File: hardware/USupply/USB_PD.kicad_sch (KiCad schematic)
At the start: 10 parts, among them Q1 Si2319CDS, U1 HUSB238

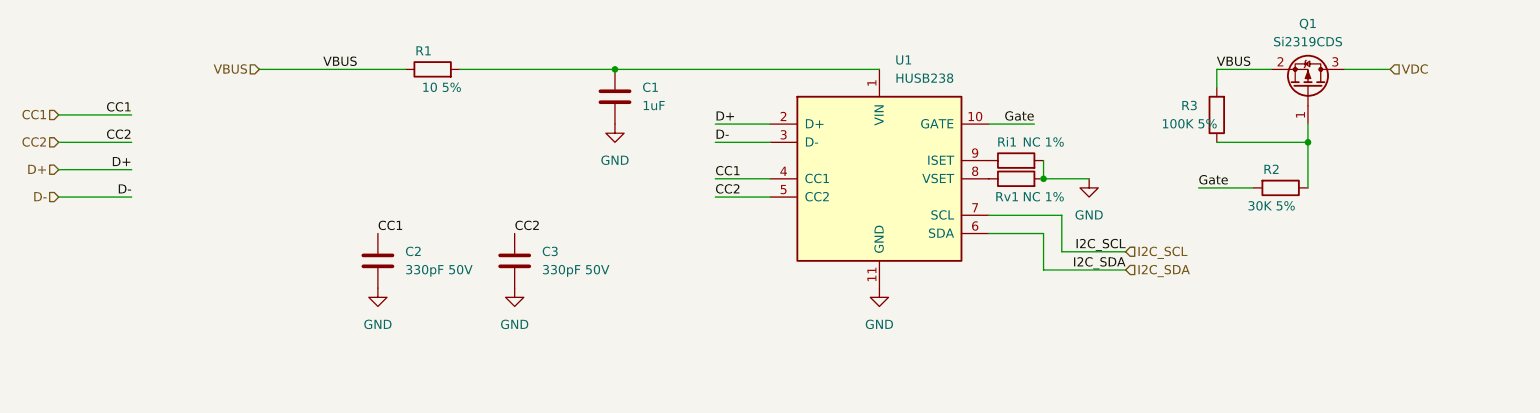
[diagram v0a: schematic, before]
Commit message: feat(hw/usb): update usb pd circuit
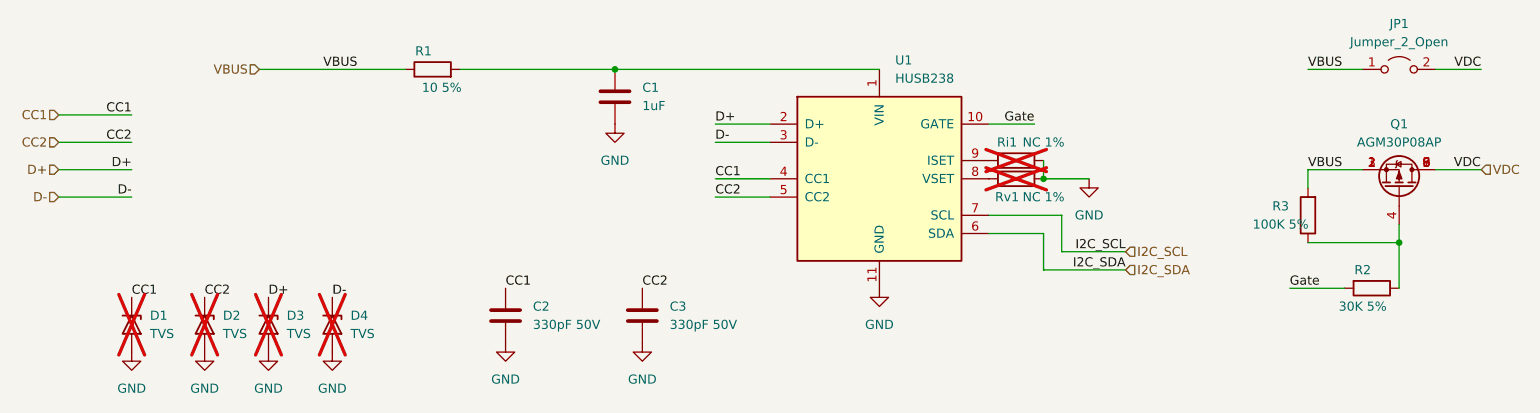
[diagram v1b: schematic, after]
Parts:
- added D1, D2, D3, D4: TVS, Diode_SMD:D_SOD-323, symbol Diode:SM6T22A
- added JP1: Jumper_2_Open, Jumper:SolderJumper-2_P1.3mm_Open_RoundedPad1.0x1.5mm, symbol Jumper:Jumper_2_Open
- Q1: value Si2319CDS -> AGM30P08AP; footprint Package_TO_SOT_SMD:SOT-23 -> Package_DFN_QFN:DFN-8-1EP_3x3mm_P0.65mm_EP1.55x2.4mm
- Ri1, Rv1: now not fitted
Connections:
- net CC1: now also D1.1 (A1)
- net CC2: now also D2.1 (A1)
- net D+: now also D3.1 (A1)
- net D-: now also D4.1 (A1)
- net GND: now also D1.2 (A2), D2.2 (A2), D3.2 (A2), D4.2 (A2)
- net VBUS: now also Q1.1 (S), Q1.3 (S), JP1.1 (A)
- net VDC: now also Q1.5 (D), Q1.6 (D), Q1.7 (D), Q1.8 (D), Q1.9 (D), JP1.2 (B); no longer Q1.3 (D)
- net at R2.1, R3.1: now also Q1.4 (G); no longer Q1.1 (G)
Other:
- moved on the sheet: C2, C3, R2, R3
